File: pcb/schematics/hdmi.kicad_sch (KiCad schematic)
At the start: 23 parts, among them J8 HDMI_A, U6 TFP410PAP, U7 ESD224DQA, U8 ESD224DQA

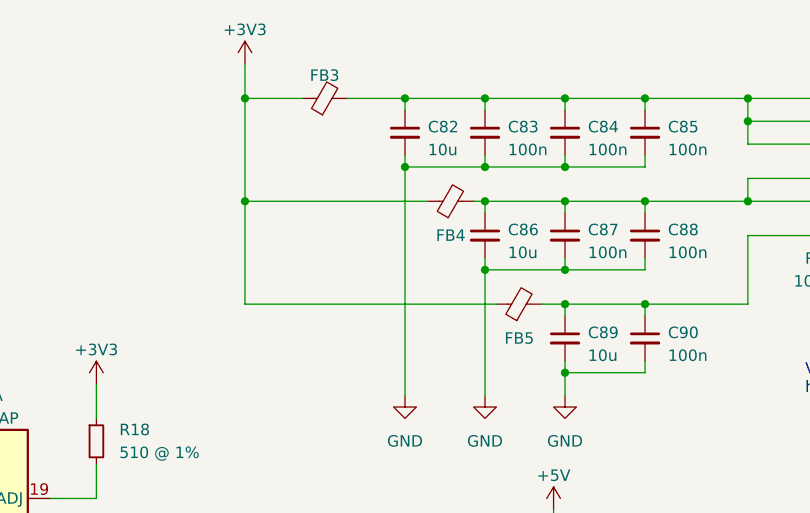
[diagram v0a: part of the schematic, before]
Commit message: place bypass caps
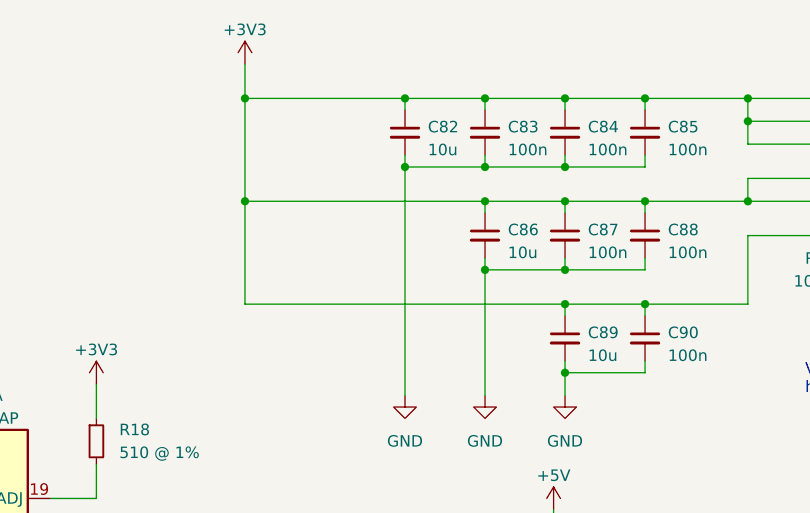
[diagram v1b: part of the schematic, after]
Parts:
- removed FB3, FB4, FB5: FerriteBead_Small, Inductor_SMD:L_0805_2012Metric, symbol Device:FerriteBead_Small
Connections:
- net +3V3: now also C82.1, C83.1, C84.1, C85.1, C86.1, C87.1, C88.1, C89.1, C90.1, U6.1 (DVDD1), U6.12 (DVDD2), U6.18 (PVDD), U6.23 (TVDD1), U6.29 (TVDD2), U6.33 (DVDD3)
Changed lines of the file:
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@@
-    (stroke (width 0) (type default))
-  )
-  (wire (pts (xy 175.26 50.8) (xy 147.32 50.8))
     (stroke (width 0) (type default))
   )
@@
     (stroke (width 0) (type default))
   )
-  (wire (pts (xy 172.72 39.37) (xy 173.99 39.37))
+  (wire (pts (xy 147.32 39.37) (xy 173.99 39.37))
     (stroke (width 0) (type default))
   )
@@
     (stroke (width 0) (type default))
   )
-  (wire (pts (xy 167.64 39.37) (xy 147.32 39.37))
-    (stroke (width 0) (type default))
-  )
   (wire (pts (xy 165.1 27.94) (xy 165.1 29.21))
     (stroke (width 0) (type default))
@@
     (stroke (width 0) (type default))
   )
-  (wire (pts (xy 147.32 27.94) (xy 153.67 27.94))
+  (wire (pts (xy 147.32 27.94) (xy 165.1 27.94))
     (stroke (width 0) (type default))
   )
@@
     (stroke (width 0) (type default))
   )
-  (wire (pts (xy 180.34 50.8) (xy 182.88 50.8))
+  (wire (pts (xy 147.32 50.8) (xy 182.88 50.8))
     (stroke (width 0) (type default))
   )
@@
   )
   (wire (pts (xy 173.99 39.37) (xy 182.88 39.37))
-    (stroke (width 0) (type default))
-  )
-  (wire (pts (xy 158.75 27.94) (xy 165.1 27.94))
     (stroke (width 0) (type default))
   )
@@
     (pin "9")
   )
-  (symbol (lib_id "Device:FerriteBead_Small") (at 177.8 50.8 90) (unit 1)
-    (in_bom yes) (on_board yes)
-    (property "Reference" "FB5" (id 0) (at 177.8 54.61 90)
-      (effects (font (size 1.27 1.27)))
-    )
-    (property "Value" "FerriteBead_Small" (id 1) (at 177.7619 48.26 90)
-      (effects (font (size 1.27 1.27)) hide)
-    )
-    (property "Footprint" "Inductor_SMD:L_0805_2012Metric" (id 2) (at 177.8 52.578 90)
-      (effects (font (size 1.27 1.27)) hide)
-    )
-    (property "Datasheet" "~" (id 3) (at 177.8 50.8 0)
-      (effects (font (size 1.27 1.27)) hide)
-    )
-    (property "Part Number" "MFBM1V2012-150-R" (id 4) (at 177.8 50.8 0)
-      (effects (font (size 1.27 1.27)) hide)
-    )
-    (pin "1")
-    (pin "2")
-  )
   (symbol (lib_id "power:+3V3") (at 130.81 59.69 0) (unit 1)
     (in_bom yes) (on_board yes) (fields_autoplaced)
@@
     (pin "9")
   )
-  (symbol (lib_id "Device:FerriteBead_Small") (at 156.21 27.94 90) (unit 1)
-    (in_bom yes) (on_board yes) (fields_autoplaced)
-    (property "Reference" "FB3" (id 0) (at 156.1719 25.4 90)
-      (effects (font (size 1.27 1.27)))
-    )
-    (property "Value" "FerriteBead_Small" (id 1) (at 156.1719 25.4 90)
-      (effects (font (size 1.27 1.27)) hide)
-    )
-    (property "Footprint" "Inductor_SMD:L_0805_2012Metric" (id 2) (at 156.21 29.718 90)
-      (effects (font (size 1.27 1.27)) hide)
-    )
-    (property "Datasheet" "~" (id 3) (at 156.21 27.94 0)
-      (effects (font (size 1.27 1.27)) hide)
-    )
-    (property "Part Number" "MFBM1V2012-150-R" (id 4) (at 156.21 27.94 0)
-      (effects (font (size 1.27 1.27)) hide)
-    )
-    (pin "1")
-    (pin "2")
-  )
   (symbol (lib_id "power:GND") (at 182.88 60.96 0) (unit 1)
     (in_bom yes) (on_board yes) (fields_autoplaced)
@@
       (effects (font (size 1.27 1.27)) hide)
     )
-    (pin "1")
-    (pin "2")
-  )
-  (symbol (lib_id "Device:FerriteBead_Small") (at 170.18 39.37 90) (unit 1)
-    (in_bom yes) (on_board yes)
-    (property "Reference" "FB4" (id 0) (at 170.18 43.18 90)
-      (effects (font (size 1.27 1.27)))
-    )
-    (property "Value" "FerriteBead_Small" (id 1) (at 170.1419 36.83 90)
-      (effects (font (size 1.27 1.27)) hide)
-    )
-    (property "Footprint" "Inductor_SMD:L_0805_2012Metric" (id 2) (at 170.18 41.148 90)
-      (effects (font (size 1.27 1.27)) hide)
-    )
-    (property "Datasheet" "~" (id 3) (at 170.18 39.37 0)
-      (effects (font (size 1.27 1.27)) hide)
-    )
-    (property "Part Number" "MFBM1V2012-150-R" (id 4) (at 170.18 39.37 0)
-      (effects (font (size 1.27 1.27)) hide)
-    )

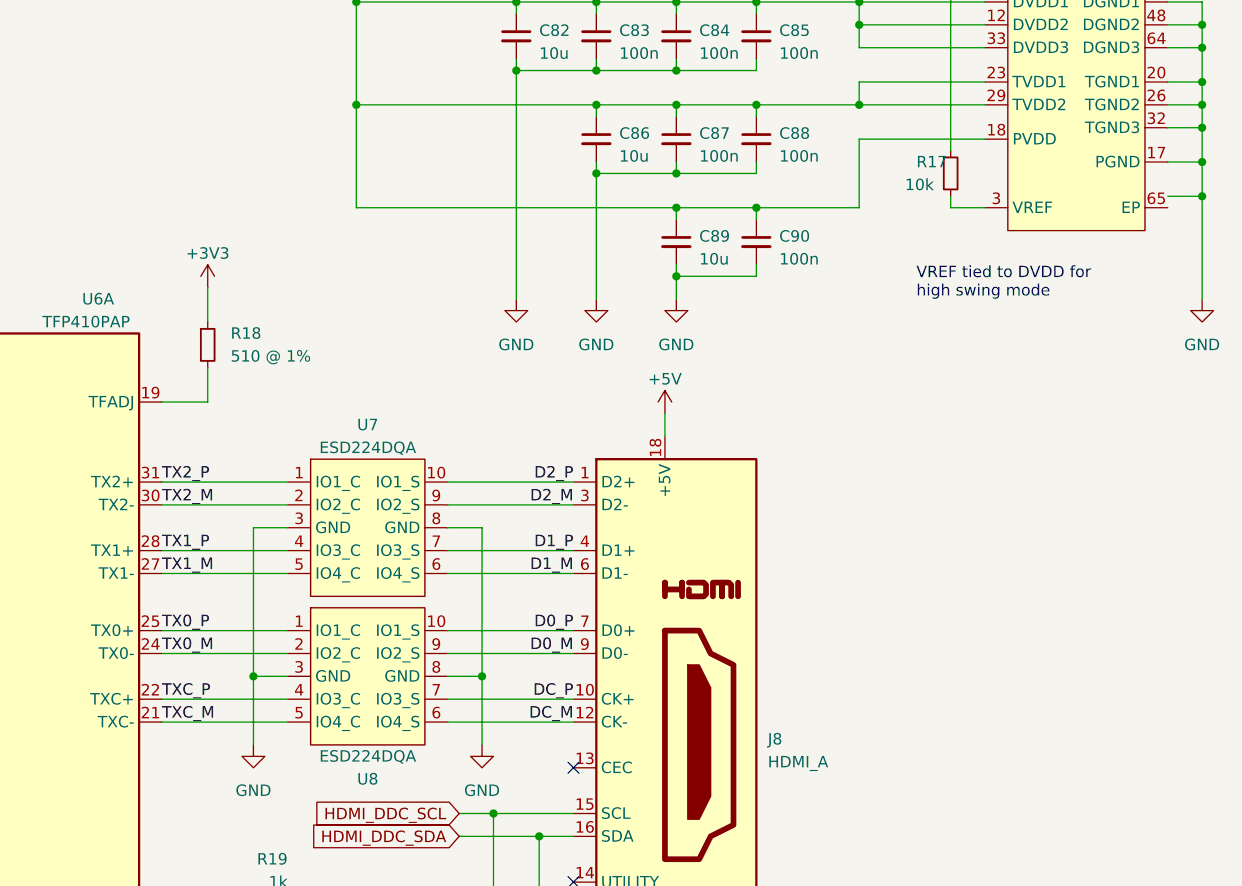
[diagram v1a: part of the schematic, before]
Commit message: change the bank for the hdmi interface
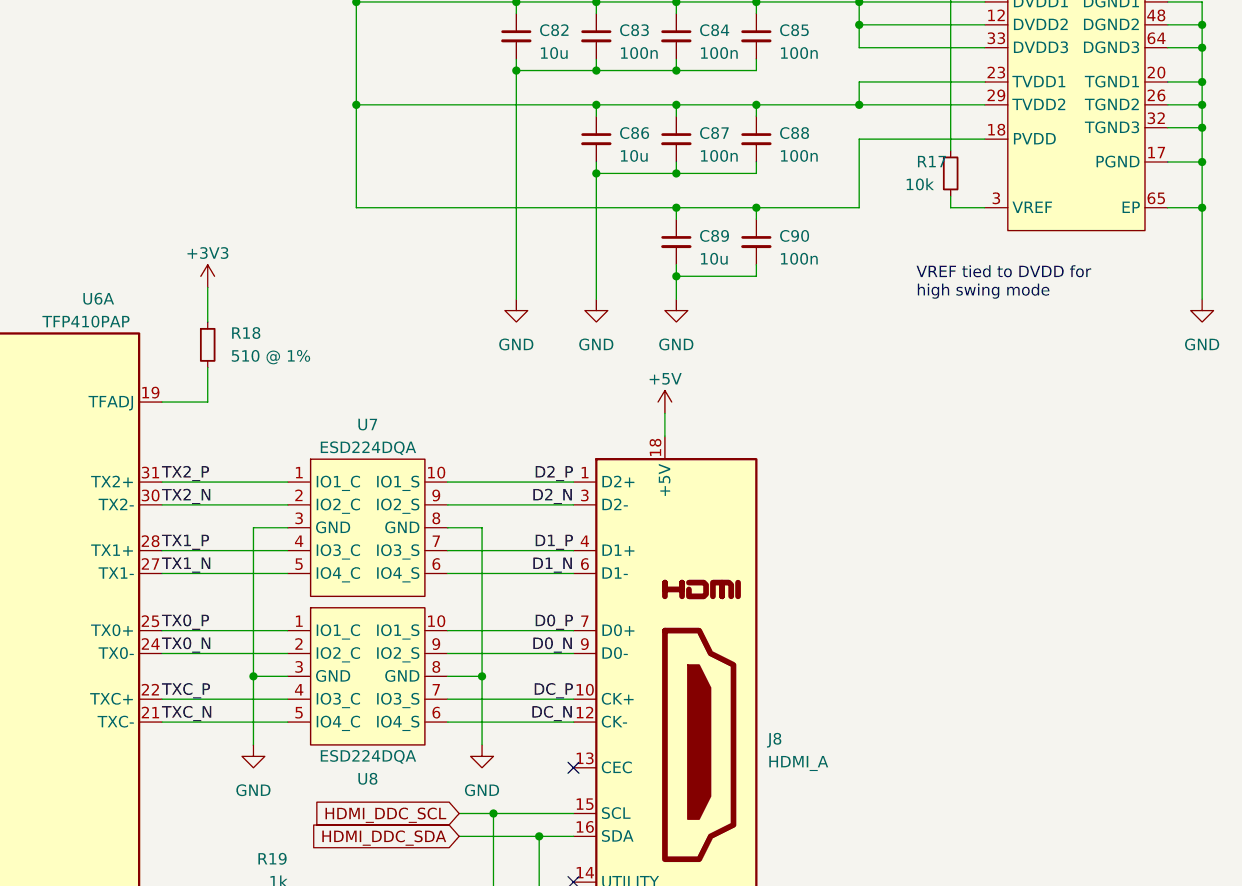
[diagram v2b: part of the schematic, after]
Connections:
- net GND: now also U6.65 (EP)
- net D0_M renamed D0_N
- net D1_M renamed D1_N
- net D2_M renamed D2_N
- net DC_M renamed DC_N
- net TX0_M renamed TX0_N
- net TX1_M renamed TX1_N
- net TX2_M renamed TX2_N
- net TXC_M renamed TXC_N
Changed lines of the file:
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@@
   (junction (at 182.88 46.99) (diameter 0) (color 0 0 0 0)
   )
+  (junction (at 241.3 50.8) (diameter 0) (color 0 0 0 0)
+  )
   (junction (at 165.1 35.56) (diameter 0) (color 0 0 0 0)
   )
@@
   )
   (junction (at 184.15 140.97) (diameter 0) (color 0 0 0 0)
-  )
-  (junction (at 241.3 49.53) (diameter 0) (color 0 0 0 0)
   )
   (junction (at 241.3 39.37) (diameter 0) (color 0 0 0 0)
@@
     (stroke (width 0) (type default))
   )
+  (wire (pts (xy 241.3 45.72) (xy 241.3 50.8))
+    (stroke (width 0) (type default))
+  )
   (wire (pts (xy 213.36 50.8) (xy 213.36 49.53))
     (stroke (width 0) (type default))
@@
     (stroke (width 0) (type default))
   )
-  (wire (pts (xy 241.3 60.96) (xy 241.3 49.53))
+  (wire (pts (xy 241.3 60.96) (xy 241.3 50.8))
     (stroke (width 0) (type default))
   )
@@
     (stroke (width 0) (type default))
   )
-  (wire (pts (xy 241.3 49.53) (xy 241.3 45.72))
-    (stroke (width 0) (type default))
-  )
   (wire (pts (xy 165.1 35.56) (xy 165.1 60.96))
     (stroke (width 0) (type default))
@@
     (stroke (width 0) (type default))
   )
-  (wire (pts (xy 237.49 49.53) (xy 241.3 49.53))
+  (wire (pts (xy 237.49 50.8) (xy 241.3 50.8))
     (stroke (width 0) (type default))
   )
@@
     (effects (font (size 1.27 1.27)) (justify left bottom))
   )
-  (label "D1_M" (at 171.45 91.44 0) (fields_autoplaced)
+  (label "D1_N" (at 171.45 91.44 0) (fields_autoplaced)
     (effects (font (size 1.27 1.27)) (justify right bottom))
   )
@@
     (effects (font (size 1.27 1.27)) (justify left bottom))
   )
-  (label "D2_M" (at 171.45 83.82 0) (fields_autoplaced)
+  (label "D2_N" (at 171.45 83.82 0) (fields_autoplaced)
     (effects (font (size 1.27 1.27)) (justify right bottom))
   )
@@
     (effects (font (size 1.27 1.27)) (justify left bottom))
   )
-  (label "TXC_M" (at 125.73 107.95 0) (fields_autoplaced)
+  (label "TXC_N" (at 125.73 107.95 0) (fields_autoplaced)
     (effects (font (size 1.27 1.27)) (justify left bottom))
   )
@@
     (effects (font (size 1.27 1.27)) (justify right bottom))
   )
-  (label "TX2_M" (at 125.73 83.82 0) (fields_autoplaced)
-    (effects (font (size 1.27 1.27)) (justify left bottom))
-  )
-  (label "TX0_M" (at 125.73 100.33 0) (fields_autoplaced)
-    (effects (font (size 1.27 1.27)) (justify left bottom))
-  )
-  (label "D0_M" (at 171.45 100.33 0) (fields_autoplaced)
+  (label "TX2_N" (at 125.73 83.82 0) (fields_autoplaced)
+    (effects (font (size 1.27 1.27)) (justify left bottom))
+  )
+  (label "TX0_N" (at 125.73 100.33 0) (fields_autoplaced)
+    (effects (font (size 1.27 1.27)) (justify left bottom))
+  )
+  (label "D0_N" (at 171.45 100.33 0) (fields_autoplaced)
     (effects (font (size 1.27 1.27)) (justify right bottom))
   )
@@
     (effects (font (size 1.27 1.27)) (justify left bottom))
   )
-  (label "TX1_M" (at 125.73 91.44 0) (fields_autoplaced)
-    (effects (font (size 1.27 1.27)) (justify left bottom))
-  )
-  (label "DC_M" (at 171.45 107.95 0) (fields_autoplaced)
-    (effects (font (size 1.27 1.27)) (justify right bottom))
-  )
+  (label "TX1_N" (at 125.73 91.44 0) (fields_autoplaced)
+    (effects (font (size 1.27 1.27)) (justify left bottom))
+  )
+  (label "DC_N" (at 171.45 107.95 0) (fields_autoplaced)
+    (effects (font (size 1.27 1.27)) (justify right bottom))
+  )

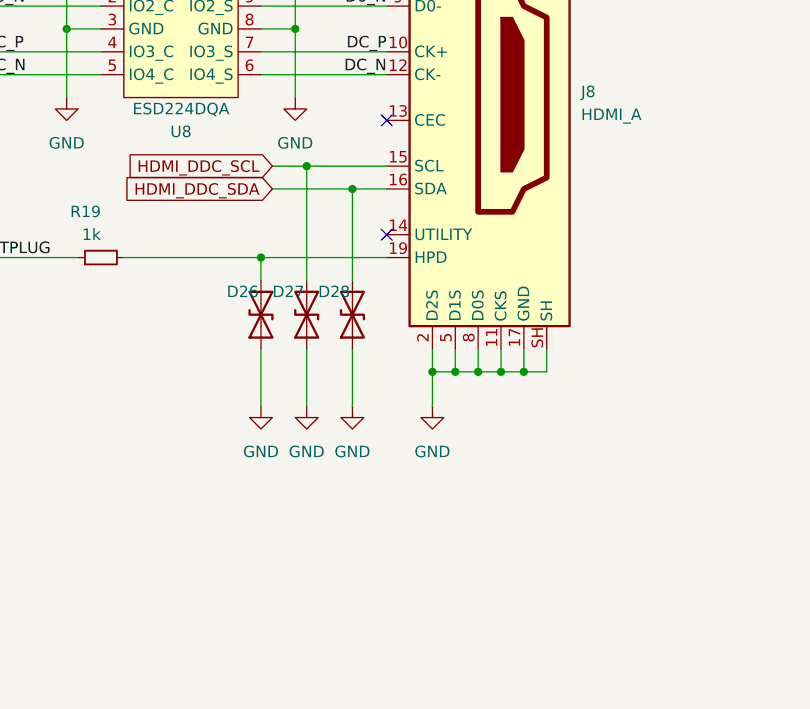
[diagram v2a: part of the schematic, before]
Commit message: add length matching to parallel buses
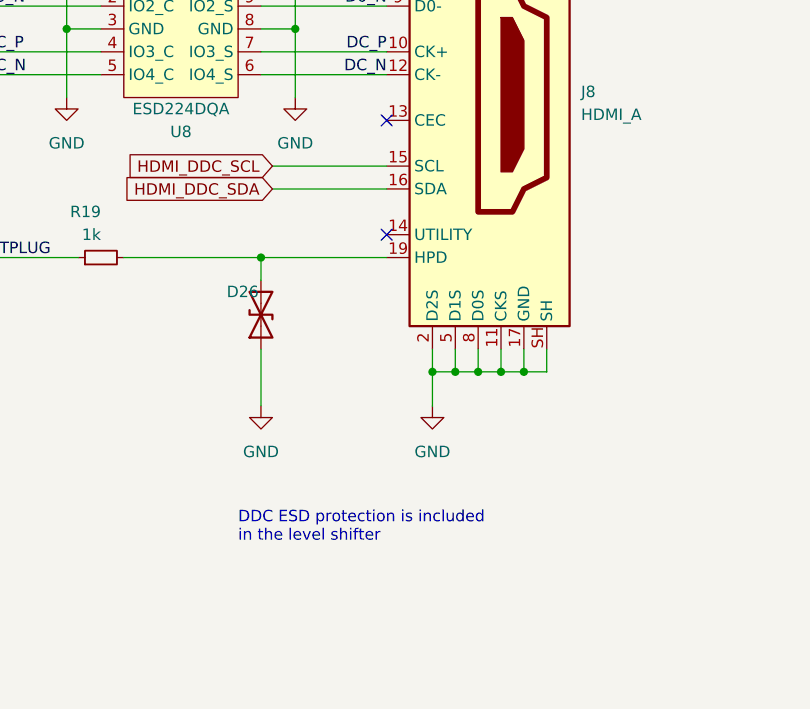
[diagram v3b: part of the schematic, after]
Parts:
- removed D27, D28: D_TVS, Diode_SMD:D_0603_1608Metric, symbol Device:D_TVS
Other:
- note added: "DDC ESD protection is included in the level shifter"
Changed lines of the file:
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@@
   (junction (at 173.99 46.99) (diameter 0) (color 0 0 0 0)
   )
-  (junction (at 162.56 118.11) (diameter 0) (color 0 0 0 0)
-  )
   (junction (at 182.88 50.8) (diameter 0) (color 0 0 0 0)
   )
@@
   )
   (junction (at 173.99 35.56) (diameter 0) (color 0 0 0 0)
-  )
-  (junction (at 167.64 120.65) (diameter 0) (color 0 0 0 0)
   )
   (junction (at 182.88 27.94) (diameter 0) (color 0 0 0 0)
@@
     (stroke (width 0) (type default))
   )
-  (wire (pts (xy 162.56 118.11) (xy 171.45 118.11))
-    (stroke (width 0) (type default))
-  )
   (wire (pts (xy 241.3 27.94) (xy 237.49 27.94))
     (stroke (width 0) (type default))
@@
     (stroke (width 0) (type default))
   )
-  (wire (pts (xy 158.75 120.65) (xy 167.64 120.65))
+  (wire (pts (xy 158.75 120.65) (xy 171.45 120.65))
     (stroke (width 0) (type default))
   )
@@
     (stroke (width 0) (type default))
   )
-  (wire (pts (xy 167.64 138.43) (xy 167.64 144.78))
-    (stroke (width 0) (type default))
-  )
   (wire (pts (xy 241.3 60.96) (xy 241.3 50.8))
     (stroke (width 0) (type default))
@@
     (stroke (width 0) (type default))
   )
-  (wire (pts (xy 167.64 130.81) (xy 167.64 120.65))
-    (stroke (width 0) (type default))
-  )
-  (wire (pts (xy 162.56 138.43) (xy 162.56 144.78))
-    (stroke (width 0) (type default))
-  )
   (wire (pts (xy 161.29 102.87) (xy 161.29 86.36))
     (stroke (width 0) (type default))
@@
     (stroke (width 0) (type default))
   )
-  (wire (pts (xy 158.75 118.11) (xy 162.56 118.11))
+  (wire (pts (xy 158.75 118.11) (xy 171.45 118.11))
     (stroke (width 0) (type default))
   )
@@
     (stroke (width 0) (type default))
   )
-  (wire (pts (xy 162.56 130.81) (xy 162.56 118.11))
-    (stroke (width 0) (type default))
-  )
   (wire (pts (xy 203.2 27.94) (xy 191.77 27.94))
     (stroke (width 0) (type default))
@@
   )
   (wire (pts (xy 181.61 138.43) (xy 181.61 140.97))
-    (stroke (width 0) (type default))
-  )
-  (wire (pts (xy 167.64 120.65) (xy 171.45 120.65))
     (stroke (width 0) (type default))
   )
@@
   (text "ISEL/~{RST} tied high to enable\nconfiguration through I2C"
     (at 40.64 175.26 0)
+    (effects (font (size 1.27 1.27)) (justify left bottom))
+  )
+  (text "DDC ESD protection is included\nin the level shifter"
+    (at 154.94 160.02 0)
     (effects (font (size 1.27 1.27)) (justify left bottom))
   )
@@
     (pin "2")
   )
-  (symbol (lib_id "power:GND") (at 162.56 144.78 0) (unit 1)
-    (in_bom yes) (on_board yes) (fields_autoplaced)
-    (property "Reference" "#PWR0111" (id 0) (at 162.56 151.13 0)
-      (effects (font (size 1.27 1.27)) hide)
-    )
-    (property "Value" "GND" (id 1) (at 162.56 149.86 0)
-      (effects (font (size 1.27 1.27)))
-    )
-    (property "Footprint" "" (id 2) (at 162.56 144.78 0)
-      (effects (font (size 1.27 1.27)) hide)
-    )
-    (property "Datasheet" "" (id 3) (at 162.56 144.78 0)
-      (effects (font (size 1.27 1.27)) hide)
-    )
-    (pin "1")
-  )
   (symbol (lib_id "power:+3V3") (at 147.32 24.13 0) (unit 1)
     (in_bom yes) (on_board yes) (fields_autoplaced)
@@
     (pin "1")
   )
-  (symbol (lib_id "Device:D_TVS") (at 162.56 134.62 90) (unit 1)
-    (in_bom yes) (on_board yes)
-    (property "Reference" "D27" (id 0) (at 158.75 132.08 90)
-      (effects (font (size 1.27 1.27)) (justify right))
-    )
-    (property "Value" "D_TVS" (id 1) (at 165.1 136.525 90)
-      (effects (font (size 1.27 1.27)) (justify right) hide)
-    )
-    (property "Footprint" "Diode_SMD:D_0603_1608Metric" (id 2) (at 162.56 134.62 0)
-      (effects (font (size 1.27 1.27)) hide)
-    )
-    (property "Datasheet" "~" (id 3) (at 162.56 134.62 0)
-      (effects (font (size 1.27 1.27)) hide)
-    )
-    (property "Part Number" "82356240030" (id 4) (at 162.56 134.62 0)
-      (effects (font (size 1.27 1.27)) hide)
-    )
-    (pin "1")
-    (pin "2")
-  )
   (symbol (lib_id "power:GND") (at 161.29 110.49 0) (unit 1)
     (in_bom yes) (on_board yes) (fields_autoplaced)
@@
     )
     (pin "1")
-  )
-  (symbol (lib_id "Device:D_TVS") (at 167.64 134.62 90) (unit 1)
-    (in_bom yes) (on_board yes)
-    (property "Reference" "D28" (id 0) (at 163.83 132.08 90)
-      (effects (font (size 1.27 1.27)) (justify right))
-    )
-    (property "Value" "D_TVS" (id 1) (at 170.18 136.525 90)
-      (effects (font (size 1.27 1.27)) (justify right) hide)
-    )
-    (property "Footprint" "Diode_SMD:D_0603_1608Metric" (id 2) (at 167.64 134.62 0)
-      (effects (font (size 1.27 1.27)) hide)
-    )
-    (property "Datasheet" "~" (id 3) (at 167.64 134.62 0)
-      (effects (font (size 1.27 1.27)) hide)
-    )
-    (property "Part Number" "82356240030" (id 4) (at 167.64 134.62 0)
-      (effects (font (size 1.27 1.27)) hide)
-    )
-    (pin "1")
-    (pin "2")
   )
   (symbol (lib_id "power:GND") (at 241.3 60.96 0) (unit 1)
@@
       (effects (font (size 1.27 1.27)) hide)
     )
-    (pin "1")
-  )
-  (symbol (lib_id "power:GND") (at 167.64 144.78 0) (unit 1)
-    (in_bom yes) (on_board yes) (fields_autoplaced)
-    (property "Reference" "#PWR0112" (id 0) (at 167.64 151.13 0)
-      (effects (font (size 1.27 1.27)) hide)
-    )
-    (property "Value" "GND" (id 1) (at 167.64 149.86 0)
-      (effects (font (size 1.27 1.27)))
-    )
-    (property "Footprint" "" (id 2) (at 167.64 144.78 0)
-      (effects (font (size 1.27 1.27)) hide)
-    )
-    (property "Datasheet" "" (id 3) (at 167.64 144.78 0)
-      (effects (font (size 1.27 1.27)) hide)
-    )
